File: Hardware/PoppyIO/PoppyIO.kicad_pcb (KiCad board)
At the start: 2 copper layers, 102 x 86 mm, 251 parts, among them J1 WAGO 233-504, J10 Phoenix MPT 0,5/ 4-2,54, J11 TC2030-IDC, J12 Conn_02x06_Odd_Even, J2 WAGO 233-504, J3 WAGO 233-504, J4 WAGO 233-504, J5 WAGO 233-504, J6 WAGO 233-504, J7 WAGO 233-504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

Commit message: hw: io: More PCB tweaks
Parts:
- added REF**: MountingHole_2.2mm_M2, MountingHole:MountingHole_2.2mm_M2, F.Cu at (175.0, 62.0)
- added REF**: MountingHole_2.2mm_M2, MountingHole:MountingHole_2.2mm_M2, F.Cu at (196.0, 62.0)
- moved REF** 29.9 mm to (175.0, 86.0)
- moved D1 23.8 mm to (195.7, 81.0), turned to 90 degrees
- moved C1 23.8 mm to (192.5, 89.2), turned to 180 degrees
- moved D2 19.7 mm to (192.5, 81.0), turned to 90 degrees
- moved JP1 14.8 mm to (187.5, 74.6), turned to 0 degrees
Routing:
- net /VSYS: track 93.2 -> 67.0 mm
- net +5V: track 38.6 -> 56.8 mm
- net Net-(D1-Pad2): track 7.92 -> 9.15 mm
- net GND: vias 107 -> 103
- net (no net): vias 0 -> 1

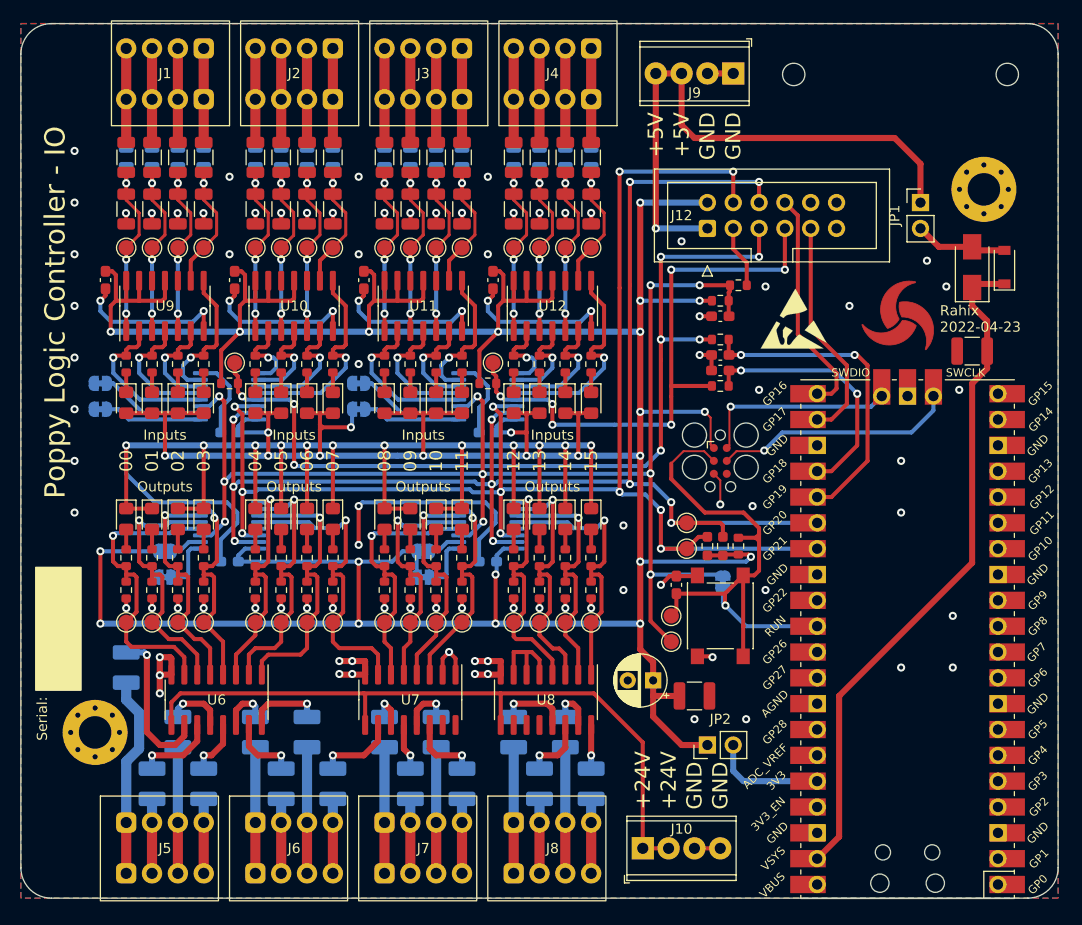
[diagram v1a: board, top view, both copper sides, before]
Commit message: hw: io: Add footprints for 24V -> 5V regulator
In the future, maybe we will want to switch to a unified 24V supply.
Add footprints for installing a regulator or SPMS to do this.
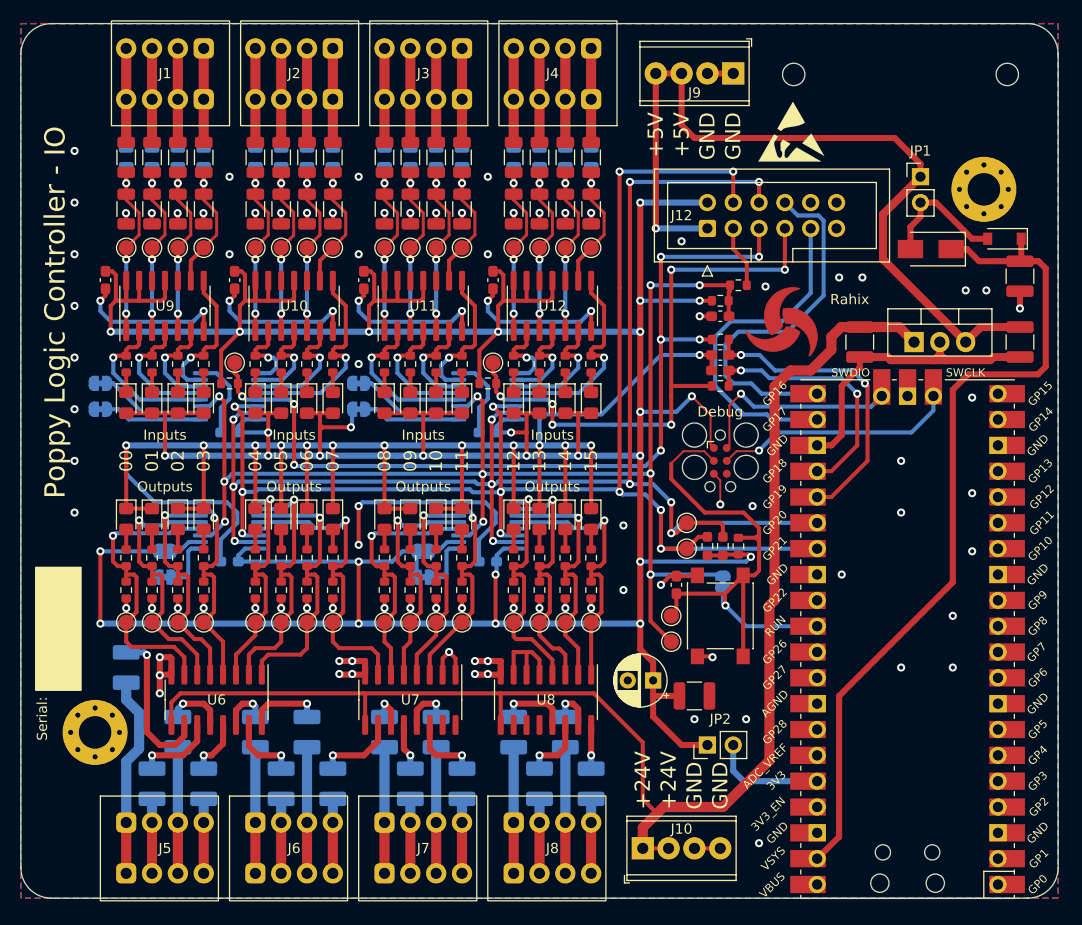
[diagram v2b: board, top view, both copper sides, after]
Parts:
- added C32: 10u, Capacitor_SMD:C_1210_3225Metric, F.Cu at (181.5, 88.3)
- added C33: 10u, Capacitor_SMD:C_1210_3225Metric, F.Cu at (197.2, 88.3)
- added U13: LM78xx, PoppyLogicController:TO-220-3_Vertical_Clearance, F.Cu at (186.8, 88.3)
- moved REF** 18.4 mm to (174.8, 67.6)
- moved REF** 13.5 mm to (173.6, 87.6)
- moved REF** 13.5 mm to (181.2, 87.6)
- moved SYM1 11.4 mm to (174.1, 86.7)
- moved C1 8.74 mm to (197.2, 81.8), turned to -90 degrees
- moved D2 4.44 mm to (188.5, 79.2), turned to 180 degrees
- moved D1 2.79 mm to (195.7, 78.2), turned to 180 degrees
- moved JP1 2.54 mm to (187.5, 72.1)
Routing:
- net +24V: track 70.2 -> 139.8 mm
- net GND: track 337.0 -> 389.5 mm, vias 103 -> 108
- net +5V: track 56.8 -> 81.4 mm
- net /VSYS: track 67.0 -> 83.7 mm
- net PICO_TX: track 22.5 -> 36.4 mm
- net PICO_RX: track 22.3 -> 33.8 mm
- net Net-(D1-Pad2): track 9.15 -> 13.1 mm
- net IO_SDA: track 145.7 -> 147.6 mm
- net +3V3: track 452.2 -> 453.6 mm
- net /SWDIO: track 19.5 -> 20.7 mm
- net Net-(C2-Pad1): track 31.4 -> 30.2 mm
- net (no net): vias 1 -> 0
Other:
- board text added: "Debug"
- board text added: "Rahix"
- board text removed: "Rahix 2022-04-23"

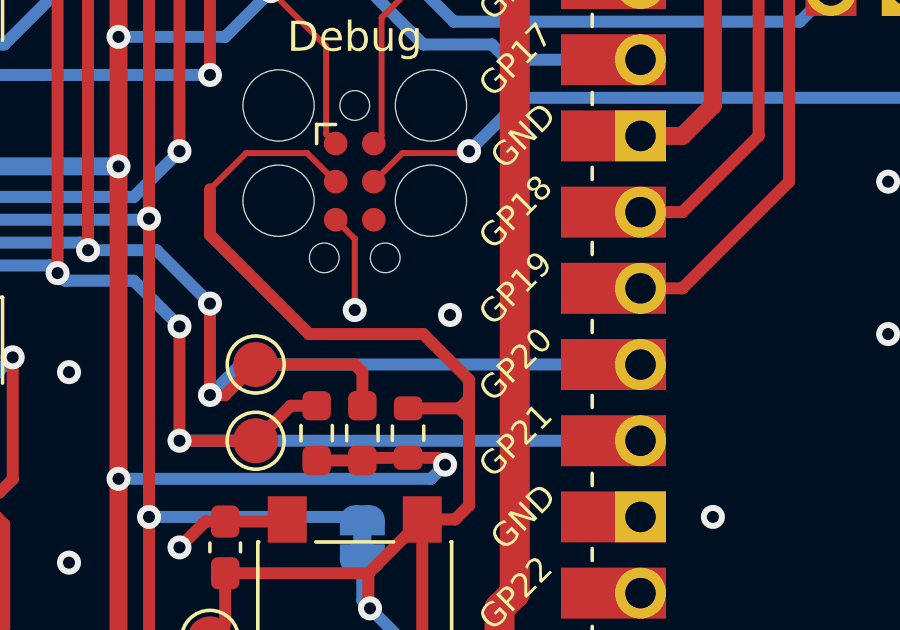
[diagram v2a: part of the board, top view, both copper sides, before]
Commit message: hw: io: pcb: Fabrication layers
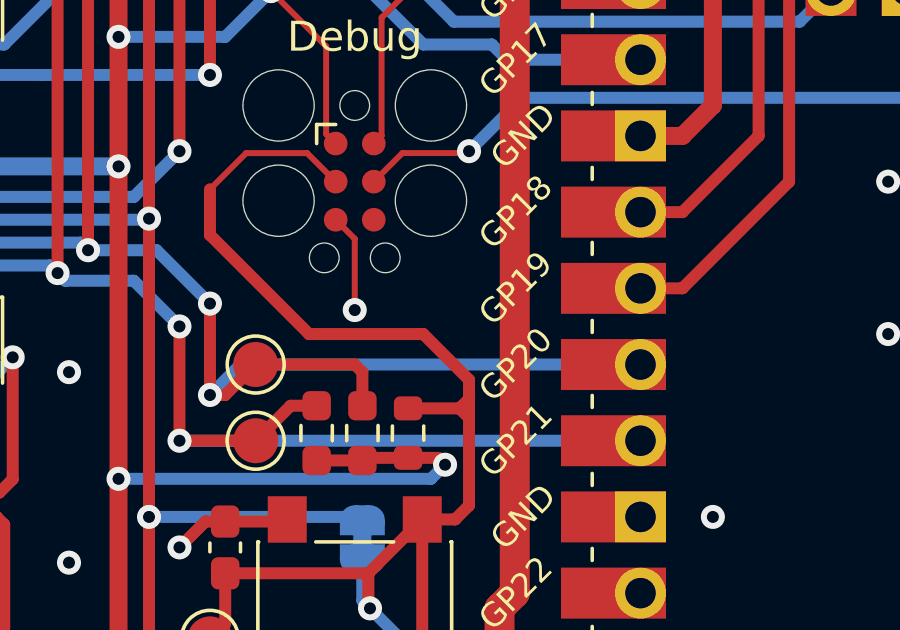
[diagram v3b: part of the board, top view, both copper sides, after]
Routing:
- net GND: vias 108 -> 107
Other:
- board text added: "entire row:"

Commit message: hw: io: Final touches and prepare revision A
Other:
- board text added: "Poppy Logic Controller - IO Rev. A 2022-04-24"

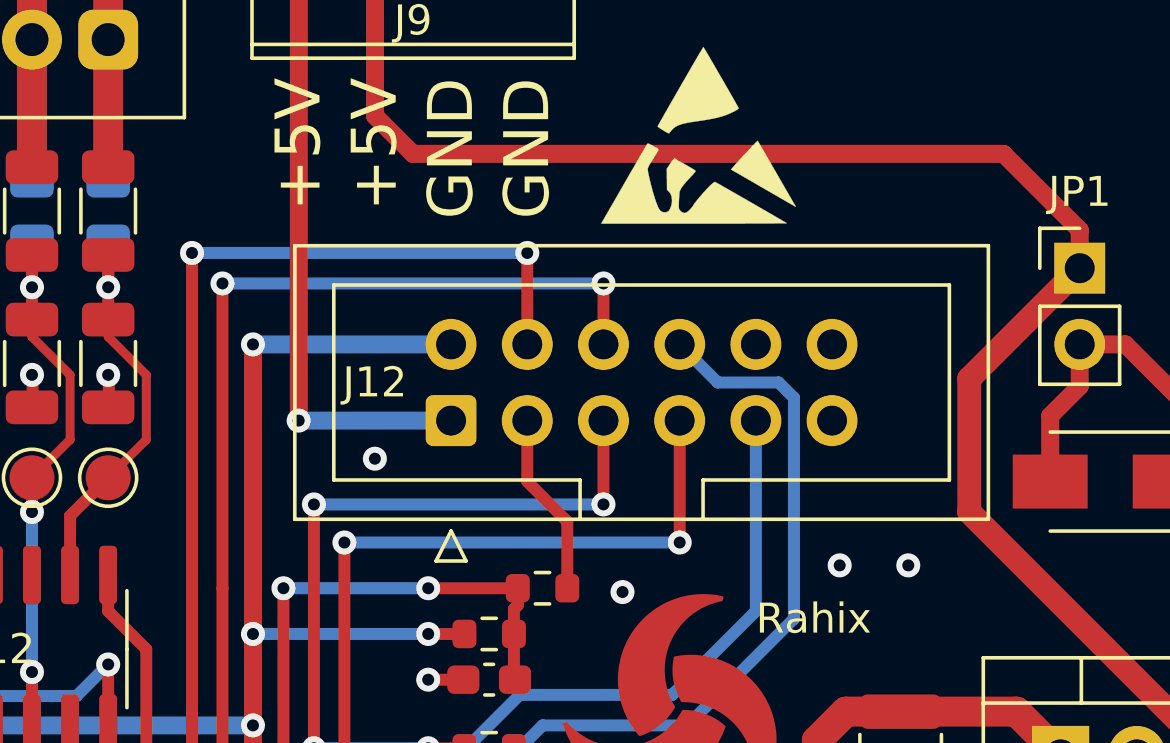
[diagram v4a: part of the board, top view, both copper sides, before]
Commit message: hw: io: Switch to 14-pin IDC
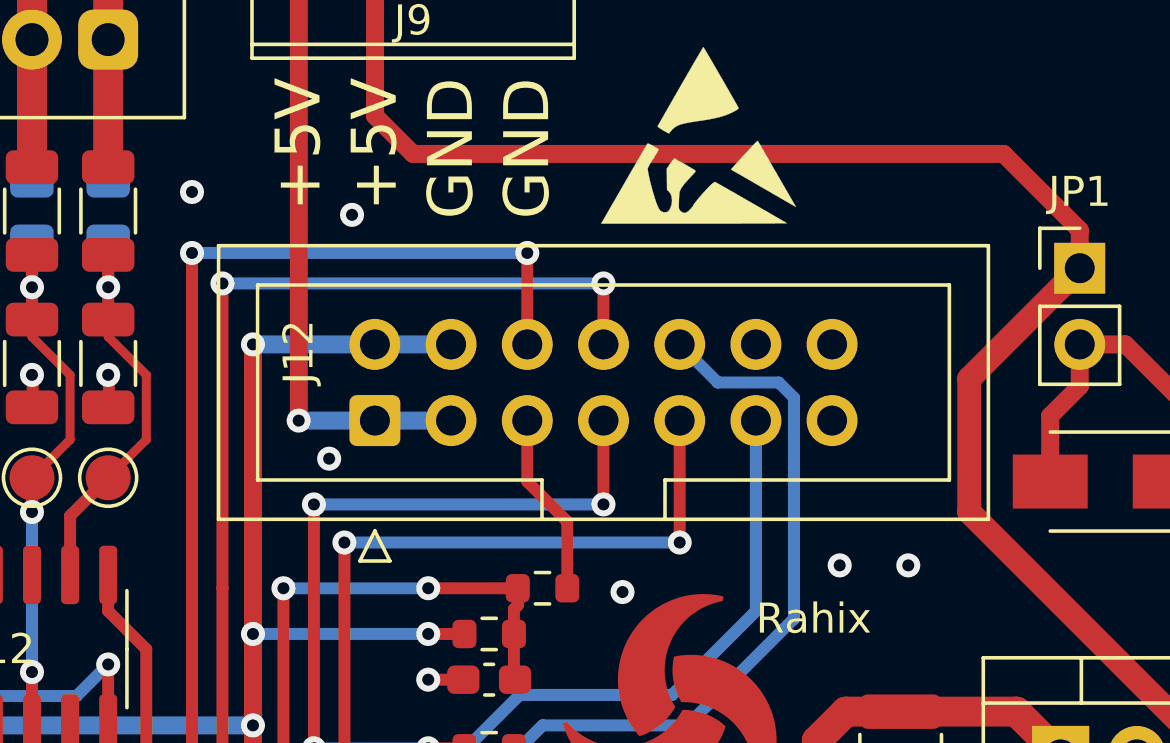
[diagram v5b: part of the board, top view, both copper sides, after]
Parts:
- J12: value Conn_02x06_Odd_Even -> Conn_02x07_Odd_Even; footprint Connector_IDC:IDC-Header_2x06_P2.54mm_Vertical -> Connector_IDC:IDC-Header_2x07_P2.54mm_Vertical
- moved J12 2.54 mm to (164.0, 77.1)
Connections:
- J12 pad 10: GND -> PICO_TX
- J12 pad 11: GND -> PICO_RX
- J12 pad 3: Net-(J12-Pad3) -> +5V
- J12 pad 4: IO_SCL -> +3V3
- J12 pad 5: IO_INT0 -> Net-(J12-Pad5)
- J12 pad 6: IO_SDA -> IO_SCL
- J12 pad 7: IO_INT1 -> IO_INT0
- J12 pad 8: PICO_TX -> IO_SDA
- J12 pad 9: PICO_RX -> IO_INT1
- R73 pad 2: Net-(J12-Pad3) -> Net-(J12-Pad5)
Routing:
- net Net-(J12-Pad5): track 0.00 -> 6.14 mm
- net Net-(J12-Pad3): track 6.14 -> 0.00 mm
- net (no net): vias 0 -> 2
